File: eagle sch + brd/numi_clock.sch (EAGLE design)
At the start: 40 parts, among them IC1 MAX7219CWG, IC2 MEGA8-AI, IC4 DS1307Z, Q1 12 MHz, Q2 32kHz, X2 MINI-USB-UX60-MB-5S8

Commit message: Fixes #1
Fixes #1
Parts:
- removed C5, C6, C7, C8: 100nF, resistor:C-EUC0805
- removed C9: 27pF, resistor:C-EUC0805
- removed HC-SR505: (no value), con-lstb:MA03-1
- removed IC3: (no value), lm75:LM75_ICN
- removed IC4: DS1307Z, ds1307_pcf8583:DS1307Z
- removed Q2: 32kHz, crystal:CRYSTALHC49U-V
- removed R12: 26k, resistor:R-EU_M0805
- removed R15, R16: 10K, resistor:R-EU_M0805
- removed SV3, SV4, SV5, SV6: (no value), con-lstb:MA09-1
- removed X2: MINI-USB-UX60-MB-5S8, con-hirose:MINI-USB-UX60-MB-5S8
- added D2: 3.6V, SparkFun-DiscreteSemi:DIODE-ZENER3.3V
- added D3: red, SparkFun-LED:LED1206
- added JP1: micro-usb, SparkFun-Connectors:USB_MICROB_PLUGCONN-11752
- added SV2: HC-SR505, con-lstb:MA03-1
- added U$1: MAX7219CWG, max7219:MAX7219CWG
- added U$2: DS1307SO8, SparkFun-FreqCtrl:DS1307SO8
- added U$3, U$4, U$5, U$6: IV-9, domestichacks:IV-9
- added Y1: 32.768kHz, SparkFun-FreqCtrl:CRYSTALTC26H
- C1: value 27pF -> 100nF; device resistor:C-EUC0805 -> rcl:C-EUC0805
- C2, C4: device resistor:C-EUC0805 -> rcl:C-EUC0805
- C3: value 100nF -> 27pF; device resistor:C-EUC0805 -> rcl:C-EUC0805
- D1: value RED -> 3.6V; device display-hp:HLMP6 -> SparkFun-DiscreteSemi:DIODE-ZENER3.3V
- IC1: value MAX7219CWG -> MEGA8-AI; device max7219:MAX7219CWG -> atmel:MEGA8-AI
- IC2: value MEGA8-AI -> LM75; device atmel:MEGA8-AI -> lm75:LM75_ICN
- Q1: value 12 MHz -> 12MHz; device crystal:CRYSTALHC49U-V -> crystal:CRYSTALHC49S
- R1, R2: device resistor:R-EU_M0805 -> rcl:R-EU_R0805
- R10, R8, R9: value 10K -> 10k; device resistor:R-EU_M0805 -> rcl:R-EU_R0805
- R11: value 10K -> 23k; device resistor:R-EU_M0805 -> rcl:R-EU_R0805
- R3: value 68 -> 1.8k; device resistor:R-EU_M0805 -> rcl:R-EU_R0805
- R4: value 1.8K -> 68; device resistor:R-EU_M0805 -> rcl:R-EU_R0805
- R5, R6: value 3v6 -> 10k; device e-halbleiter:Z-DIODE -> rcl:R-EU_R0805
- R7: value 330 -> 10k; device resistor:R-EU_M0805 -> rcl:R-EU_R0805
- S1, S2: value SWITCH-MOMENTARY-2SMD -> SWITCH-MOMENTARY-2TACTILE-SWITCH-SMD-RIGHT-ANGLE; device SparkFun-Electromechanical:SWITCH-MOMENTARY-2SMD -> SparkFun-Electromechanical:SWITCH-MOMENTARY-2TACTILE-SWITCH-SMD-RIGHT-ANGLE
- SL1: value (none) -> VBATT
- SV1: value (none) -> SPI
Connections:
- removed net CLK: IC1.CLK
- removed net N$12: R1.1
- removed net N$14: C9.1, IC3.VCC
- removed net N$15: IC2.VCC@1
- removed net N$16: R11.2
- removed net N$17: IC1.ISET, R12.2
- removed net N$18: IC2.PB7(XTAL2/TOSC2)
- removed net N$19: IC2.PB6(XTAL1/TOSC1)
- removed net N$20: IC2.PD3(INT1)
- removed net N$21: R9.2
- removed net N$22: R8.1
- removed net N$23: R6.A
- removed net N$24: R5.C
- removed net N$26: R6.C
- removed net N$28: SL1.2
- removed net N$29: C2.1
- removed net N$30: D1.K, R7.1
- removed net N$31: SV1.2
- removed net N$32: R1.2
- removed net N$35: IC4.X2, Q2.1
- removed net N$36: IC4.X1, Q2.2
- removed net N$39: IC3.GND
- removed net N$42: IC1.GND@1, IC1.GND@2
- removed net N$45: SV3.6
- removed net N$48: IC3.A2
- removed net N$6: R2.1, X2.3
- new net N$10: IC1.PD3(INT1), R2.2
- new net N$8: D1.C, JP1.D-, R2.1, R3.2
- net +3V3: now also R5.1, R6.1, R7.1, R9.1, S1.1, SL1.2, U$2.VBATT; no longer IC4.VBAT, R11.1, S2.1
- net +5V: now also D3.A, IC1.AREF, IC1.AVCC, IC1.VCC@1, IC1.VCC@2, IC2.VCC, JP1.VCC, R1.2, R10.1, R11.1, R3.1, R8.1, SV1.2, SV2.1, U$1.VCC, U$2.VCC; no longer C3.2, C5.2, C6.2, C8.2, D1.A, IC1.VCC, IC2.AREF, IC2.AVCC, IC2.VCC@2, IC4.VCC, R12.1, R15.1, R16.1, R4.1, X2.1
- net A: now also U$1.SEGA, U$3.5, U$4.5, U$5.5, U$6.5; no longer IC1.SEGA, SV3.8, SV4.8, SV5.8, SV6.8
- net B: now also U$1.SEGB, U$3.3, U$4.3, U$5.3, U$6.3; no longer IC1.SEGB, SV3.7, SV4.7, SV5.7, SV6.7
- net C: now also U$1.SEGC, U$3.4, U$4.4, U$5.4, U$6.4; no longer IC1.SEGC, SV4.6, SV5.6, SV6.6
- net CS: now also IC1.PC1(ADC1), U$1.LOAD; no longer IC1.LOAD, IC2.PC1(ADC1)
- net D: now also U$1.SEGD, U$3.8, U$4.8, U$5.8, U$6.8; no longer IC1.SEGD, SV3.5, SV4.5, SV5.5, SV6.5
- net DIG0: now also R9.2, U$1.DIG0, U$6.1; no longer IC1.DIG0, SV3.9
- net DIG1: now also R7.2, U$1.DIG1, U$5.1; no longer IC1.DIG1
- net DIG2: now also R6.2, U$1.DIG2, U$4.1; no longer IC1.DIG2, SV5.9
- net DIG3: now also R5.2, U$1.DIG3, U$3.1; no longer IC1.DIG3, R8.2, SV6.9
- net DP: now also U$1.SEGDP, U$3.2, U$4.2, U$5.2, U$6.2; no longer IC1.SEGDP, SV3.1, SV4.1, SV5.1, SV6.1
- net E: now also U$1.SEGE, U$3.9, U$4.9, U$5.9, U$6.9; no longer IC1.SEGE, SV3.4, SV4.4, SV5.4, SV6.4
- net F: now also U$1.SEGF, U$3.6, U$4.6, U$5.6, U$6.6; no longer IC1.SEGF, SV3.3, SV4.3, SV5.3, SV6.3
- net G: now also U$1.SEGG, U$3.7, U$4.7, U$5.7, U$6.7; no longer IC1.SEGG, SV3.2, SV4.2, SV5.2, SV6.2
- net GND: now also C2.1, D1.A, D2.A, D3.C, IC1.GND, IC1.GND@1, IC1.GND@2, IC2.A0, IC2.A1, IC2.A2, JP1.GND, JP1.ID, SV2.3, U$1.GND@1, U$1.GND@2, U$2.GND; no longer C5.1, C6.1, C7.1, C8.1, C9.2, HC-SR505.3, IC2.GND@1, IC2.GND@2, IC3.A0, IC3.A1, IC4.GND, R5.A, R7.2
- net HC: now also IC1.PC0(ADC0), SV2.2; no longer HC-SR505.2, IC2.PC0(ADC0)
- net MISO: now also IC1.PB4(MISO)
- net MOSI: now also IC1.PB3(MOSI/OC2), U$1.DIN; no longer IC1.DIN
- net N$1: now also C2.2, IC1.PB6(XTAL1/TOSC1); no longer C1.2
- net N$2: now also C3.2, IC1.PB7(XTAL2/TOSC2); no longer C2.2
- net N$3: now also R11.2, U$1.ISET; no longer HC-SR505.1
- net N$4: now also U$2.X1, Y1.2; no longer R3.2
- net N$5: now also U$2.X2, Y1.1; no longer S1.1
- net N$7: now also D2.C, JP1.D+, R4.1; no longer R3.1, R4.2, X2.2
- net N$9: now also IC1.PD2(INT0), R4.2; no longer IC2.PD2(INT0), R2.2
- net RESET: now also C1.2, IC1.PC6(/RESET), R1.1, S2.1; no longer C7.2, IC2.PC6(/RESET)
- net SCK: now also IC1.PB5(SCK), U$1.CLK
- net SCL: now also IC2.SCL, R10.2, U$2.SCL; no longer IC2.PC5(ADC5/SCL), IC3.SCL, IC4.SCL, R16.2
- net SDA: now also IC2.SDA, R8.2, U$2.SDA; no longer IC2.PC4(ADC4/SDA), IC3.SDA, IC4.SDA, R15.2
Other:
- moved on the sheet: C1, C2, C3, C4, Q1, R1, R10, R11, R2, R3, R4, R7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

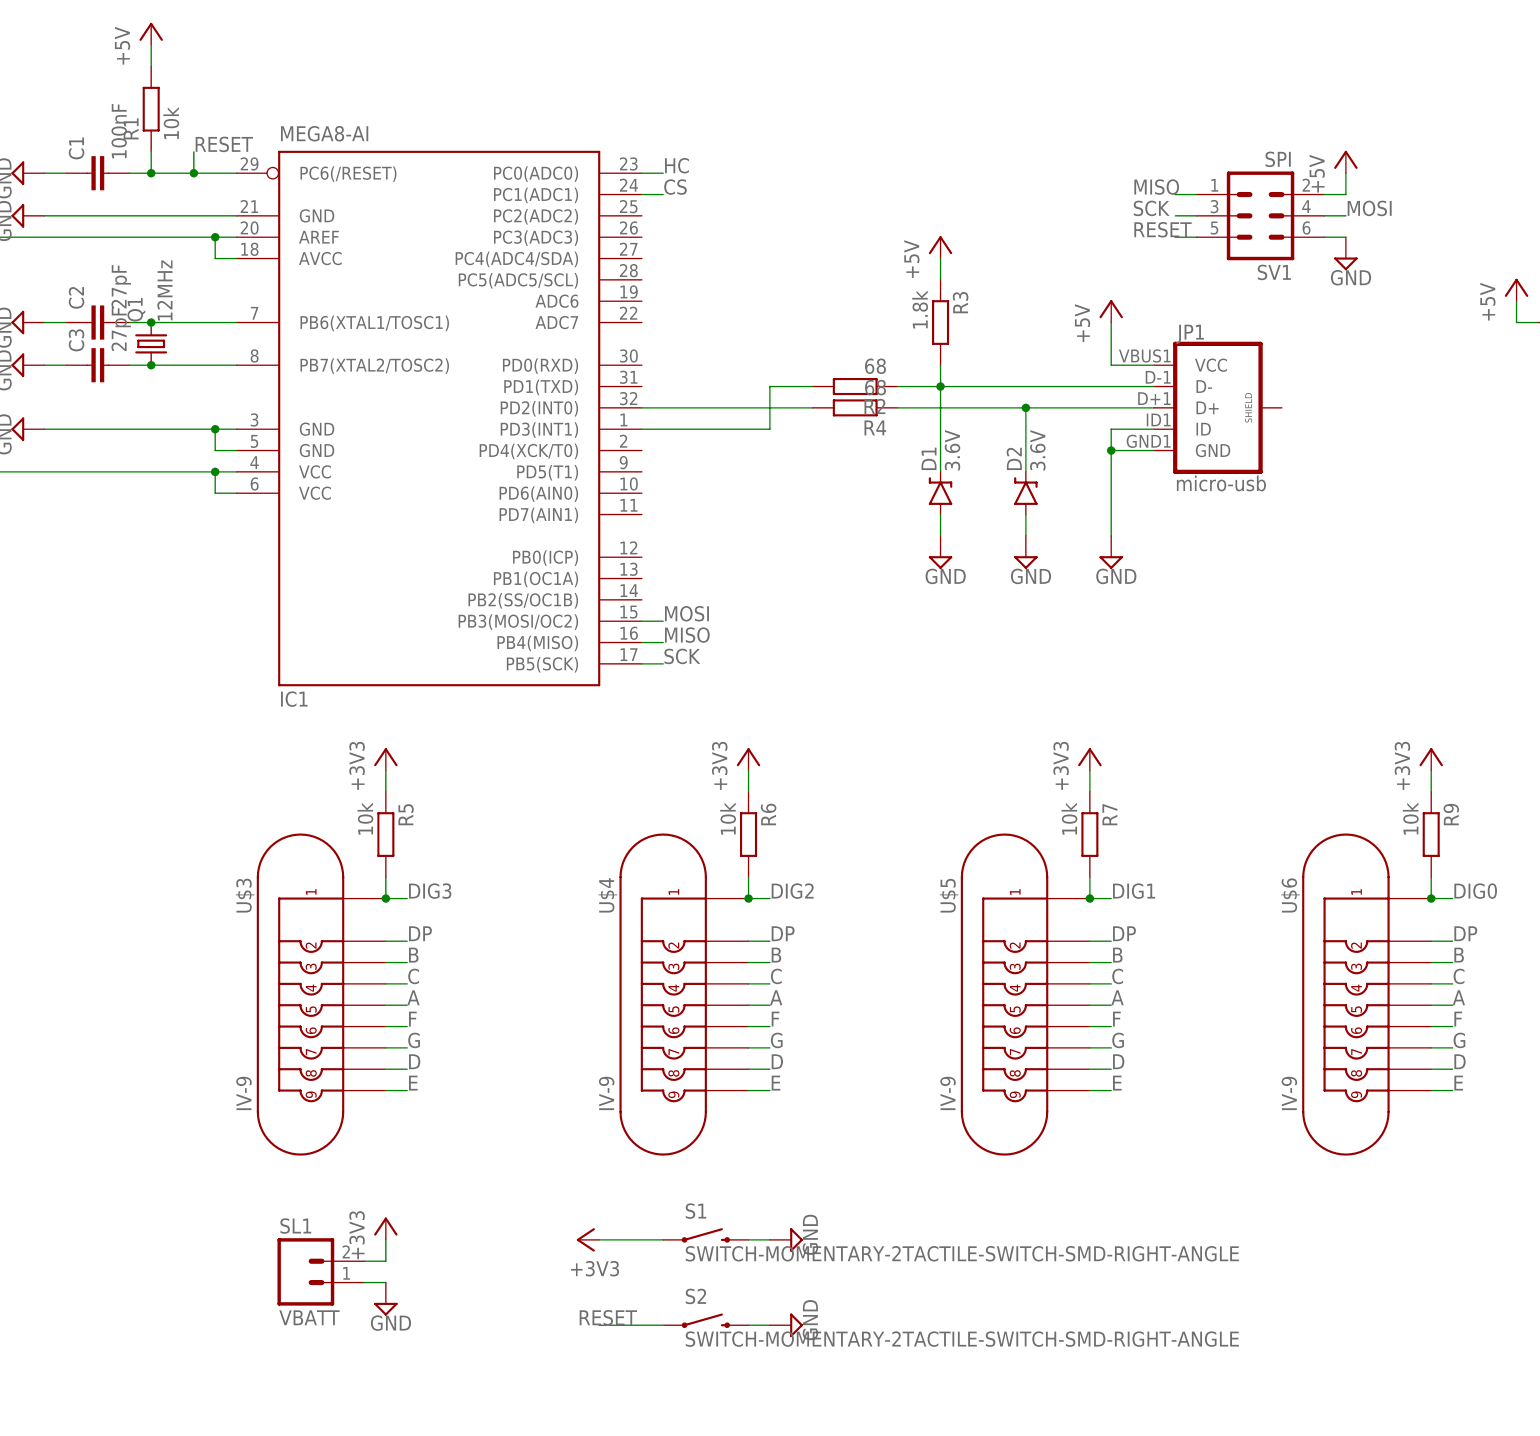
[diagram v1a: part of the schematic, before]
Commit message: added buttons for hour, minute, function
added buttons for hour, minute, function
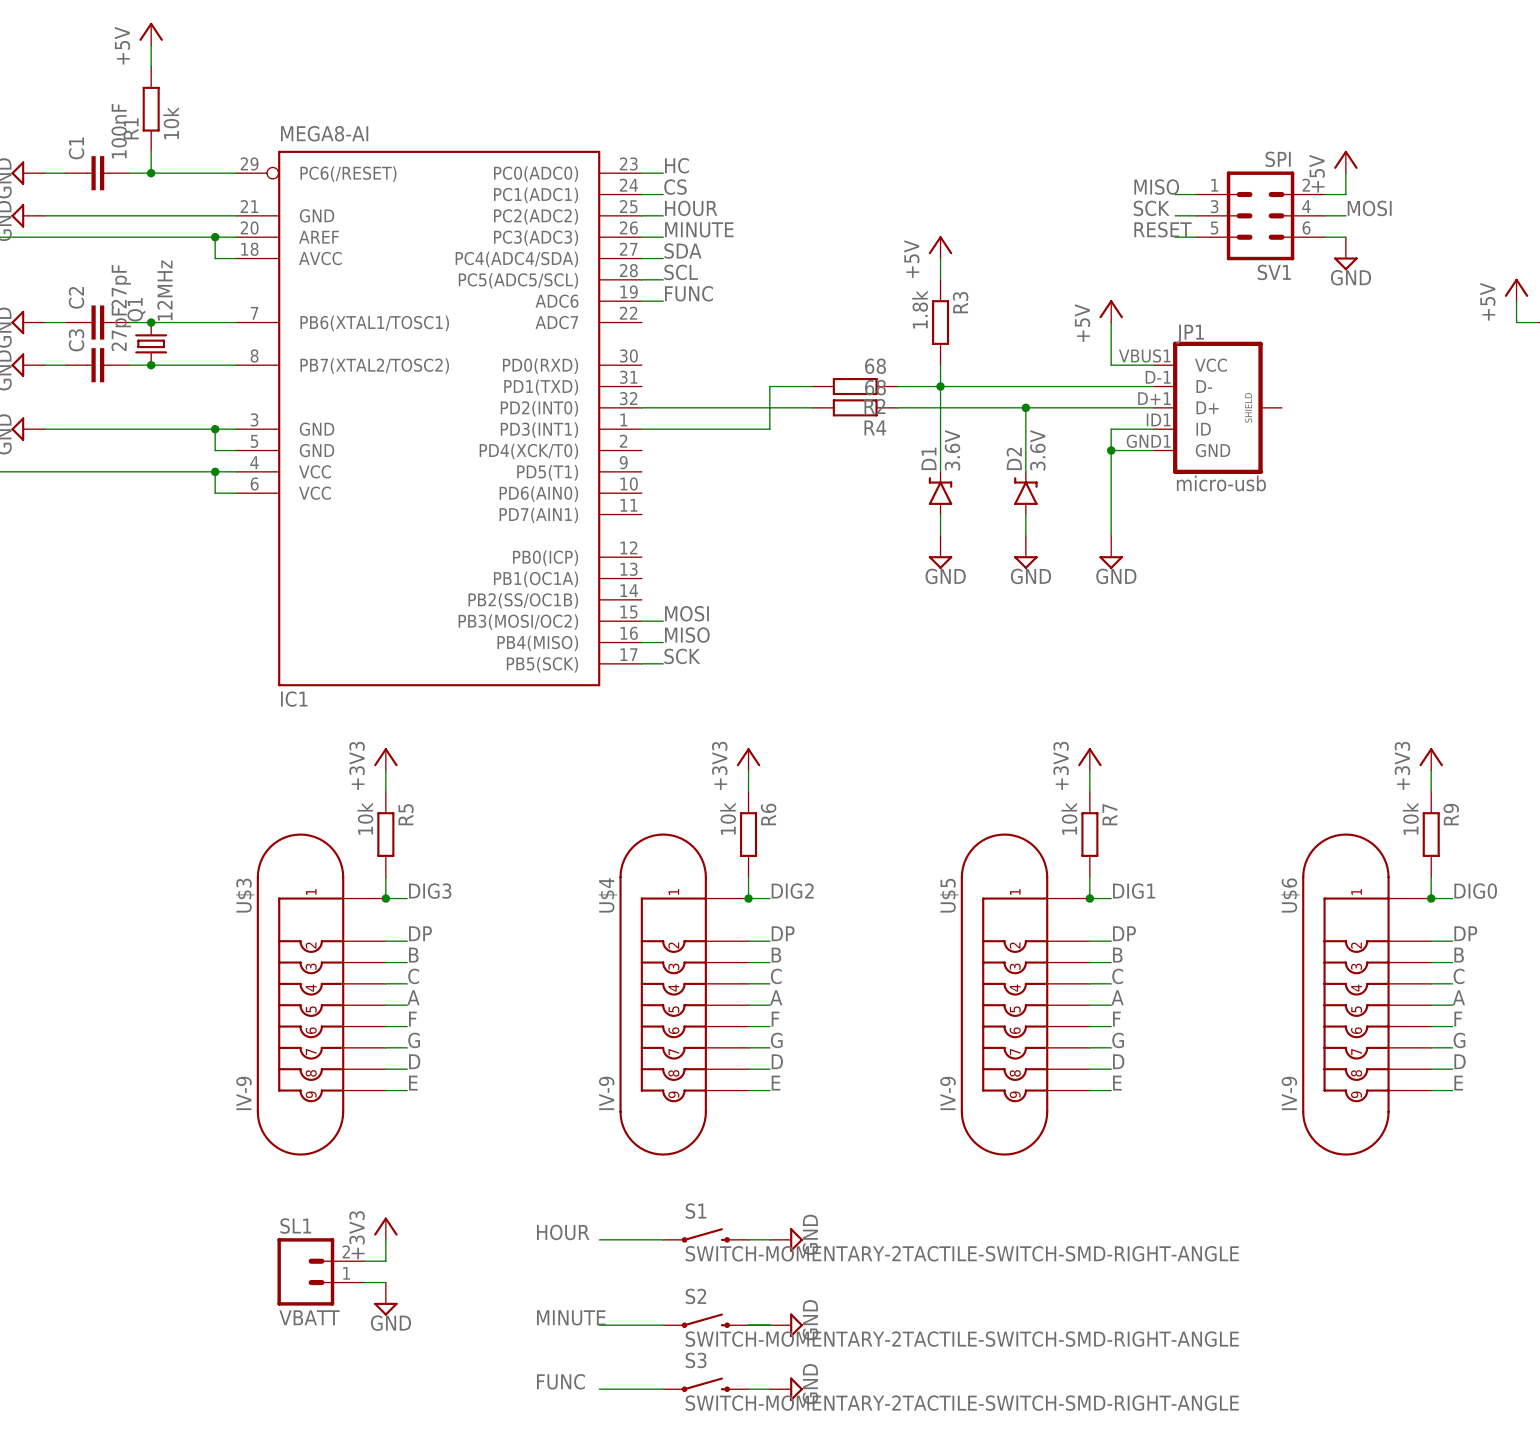
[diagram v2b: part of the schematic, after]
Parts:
- added S3: SWITCH-MOMENTARY-2TACTILE-SWITCH-SMD-RIGHT-ANGLE, SparkFun-Electromechanical:SWITCH-MOMENTARY-2TACTILE-SWITCH-SMD-RIGHT-ANGLE
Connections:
- new net FUNC: IC1.ADC6, S3.1
- new net HOUR: IC1.PC2(ADC2), S1.1
- new net MINUTE: IC1.PC3(ADC3), S2.1
- net +3V3: no longer S1.1
- net GND: now also S3.2
- net RESET: no longer S2.1
- net SCL: now also IC1.PC5(ADC5/SCL)
- net SDA: now also IC1.PC4(ADC4/SDA)
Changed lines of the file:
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@@
 <part name="S1" library="SparkFun-Electromechanical" deviceset="SWITCH-MOMENTARY-2" device="TACTILE-SWITCH-SMD-RIGHT-ANGLE"/>
 <part name="S2" library="SparkFun-Electromechanical" deviceset="SWITCH-MOMENTARY-2" device="TACTILE-SWITCH-SMD-RIGHT-ANGLE"/>
-<part name="+3V7" library="supply1" deviceset="+3V3" device=""/>
 <part name="SUPPLY17" library="supply2" deviceset="GND" device=""/>
 <part name="SUPPLY18" library="supply2" deviceset="GND" device=""/>
 <part name="R11" library="rcl" deviceset="R-EU_" device="R0805" value="23k"/>
 <part name="P+13" library="supply1" deviceset="+5V" device=""/>
+<part name="S3" library="SparkFun-Electromechanical" deviceset="SWITCH-MOMENTARY-2" device="TACTILE-SWITCH-SMD-RIGHT-ANGLE"/>
+<part name="SUPPLY19" library="supply2" deviceset="GND" device=""/>
 </parts>
 <sheets>
@@
 <instance part="S1" gate="G$1" x="-71.12" y="17.78"/>
 <instance part="S2" gate="G$1" x="-71.12" y="7.62"/>
-<instance part="+3V7" gate="G$1" x="-86.36" y="17.78" rot="R90"/>
 <instance part="SUPPLY17" gate="GND" x="-60.96" y="17.78" rot="R90"/>
 <instance part="SUPPLY18" gate="GND" x="-60.96" y="7.62" rot="R90"/>
 <instance part="R11" gate="G$1" x="33.02" y="127"/>
 <instance part="P+13" gate="1" x="25.4" y="132.08"/>
+<instance part="S3" gate="G$1" x="-71.12" y="0"/>
+<instance part="SUPPLY19" gate="GND" x="-60.96" y="0" rot="R90"/>
 </instances>
 <busses>
@@
 <pinref part="SUPPLY18" gate="GND" pin="GND"/>
 <wire x1="-66.04" y1="7.62" x2="-63.5" y2="7.62" width="0.1524" layer="91"/>
+<wire x1="-66.04" y1="7.62" x2="-63.5" y2="7.62" width="0.1524" layer="91"/>
+</segment>
+<segment>
+<pinref part="SUPPLY19" gate="GND" pin="GND"/>
+<pinref part="S3" gate="G$1" pin="2"/>
+<wire x1="-63.5" y1="0" x2="-66.04" y2="0" width="0.1524" layer="91"/>
 </segment>
 </net>
@@
 </segment>
 <segment>
-<pinref part="S2" gate="G$1" pin="1"/>
-<wire x1="-76.2" y1="7.62" x2="-83.82" y2="7.62" width="0.1524" layer="91"/>
-<label x="-86.36" y="7.62" size="1.778" layer="95"/>
-</segment>
-<segment>
 <pinref part="C1" gate="G$1" pin="2"/>
 <pinref part="IC1" gate="G$1" pin="PC6(/RESET)"/>
 <wire x1="-139.7" y1="144.78" x2="-137.16" y2="144.78" width="0.1524" layer="91"/>
 <pinref part="R1" gate="G$1" pin="1"/>
-<wire x1="-137.16" y1="144.78" x2="-132.08" y2="144.78" width="0.1524" layer="91"/>
-<wire x1="-132.08" y1="144.78" x2="-127" y2="144.78" width="0.1524" layer="91"/>
+<wire x1="-137.16" y1="144.78" x2="-127" y2="144.78" width="0.1524" layer="91"/>
 <wire x1="-137.16" y1="147.32" x2="-137.16" y2="144.78" width="0.1524" layer="91"/>
-<wire x1="-132.08" y1="144.78" x2="-132.08" y2="147.32" width="0.1524" layer="91"/>
-<label x="-132.08" y="147.32" size="1.778" layer="95"/>
-<junction x="-132.08" y="144.78"/>
 <junction x="-137.16" y="144.78"/>
 </segment>
@@
 <label x="78.74" y="50.8" size="1.778" layer="95" rot="R90"/>
 </segment>
+<segment>
+<pinref part="IC1" gate="G$1" pin="PC4(ADC4/SDA)"/>
+<wire x1="-78.74" y1="134.62" x2="-76.2" y2="134.62" width="0.1524" layer="91"/>
+<label x="-76.2" y="134.62" size="1.778" layer="95"/>
+</segment>
 </net>
 <net name="SCL" class="0">
@@
 <wire x1="86.36" y1="58.42" x2="86.36" y2="53.34" width="0.1524" layer="91"/>
 <label x="88.9" y="50.8" size="1.778" layer="95" rot="R90"/>
+</segment>
+<segment>
+<pinref part="IC1" gate="G$1" pin="PC5(ADC5/SCL)"/>
+<wire x1="-78.74" y1="132.08" x2="-76.2" y2="132.08" width="0.1524" layer="91"/>
+<label x="-76.2" y="132.08" size="1.778" layer="95"/>
 </segment>
 </net>
@@
 <wire x1="-111.76" y1="15.24" x2="-109.22" y2="15.24" width="0.1524" layer="91"/>
 <wire x1="-109.22" y1="15.24" x2="-109.22" y2="17.78" width="0.1524" layer="91"/>
-</segment>
-<segment>
-<pinref part="+3V7" gate="G$1" pin="+3V3"/>
-<pinref part="S1" gate="G$1" pin="1"/>
-<wire x1="-83.82" y1="17.78" x2="-76.2" y2="17.78" width="0.1524" layer="91"/>
 </segment>
 <segment>
@@
 </segment>
 </net>
+<net name="HOUR" class="0">
+<segment>
+<pinref part="S1" gate="G$1" pin="1"/>
+<wire x1="-83.82" y1="17.78" x2="-76.2" y2="17.78" width="0.1524" layer="91"/>
+<label x="-91.44" y="17.78" size="1.778" layer="95"/>
+</segment>
+<segment>
+<pinref part="IC1" gate="G$1" pin="PC2(ADC2)"/>
+<wire x1="-78.74" y1="139.7" x2="-76.2" y2="139.7" width="0.1524" layer="91"/>
+<label x="-76.2" y="139.7" size="1.778" layer="95"/>
+</segment>
+</net>
+<net name="FUNC" class="0">
+<segment>
+<pinref part="S3" gate="G$1" pin="1"/>
+<wire x1="-76.2" y1="0" x2="-83.82" y2="0" width="0.1524" layer="91"/>
+<label x="-91.44" y="0" size="1.778" layer="95"/>
+</segment>
+<segment>
+<pinref part="IC1" gate="G$1" pin="ADC6"/>
+<wire x1="-78.74" y1="129.54" x2="-76.2" y2="129.54" width="0.1524" layer="91"/>
+<label x="-76.2" y="129.54" size="1.778" layer="95"/>
+</segment>
+</net>
+<net name="MINUTE" class="0">
+<segment>
+<pinref part="S2" gate="G$1" pin="1"/>
+<wire x1="-76.2" y1="7.62" x2="-83.82" y2="7.62" width="0.1524" layer="91"/>
+<label x="-91.44" y="7.62" size="1.778" layer="95"/>
+</segment>
+<segment>
+<pinref part="IC1" gate="G$1" pin="PC3(ADC3)"/>
+<wire x1="-78.74" y1="137.16" x2="-76.2" y2="137.16" width="0.1524" layer="91"/>
+<label x="-76.2" y="137.16" size="1.778" layer="95"/>
+</segment>
+</net>

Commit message: minor changes
minor changes
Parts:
- removed SL1: VBATT, con-amp-quick:MA02
- added BAT2: cr2032, SparkFun:BATTERY20PTH
- added C5, C6, C7, C8: 100nF, rcl:C-EUC0805
- added D4: red, SparkFun-LED:LED1206
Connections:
- removed net +3V3: R5.1, R6.1, R7.1, R9.1, SL1.2, U$2.VBATT
- new net LED: D4.A, IC1.ADC7
- new net N$6: BAT2.+, U$2.VBATT
- net +5V: now also C5.2, C6.2, C7.2, C8.2, R5.1, R6.1, R7.1, R9.1
- net GND: now also BAT2.-, C5.1, C6.1, C7.1, C8.1, D4.C; no longer SL1.1

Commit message: layout adjustments
layout adjustments
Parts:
- removed R5, R6, R7: 10k, rcl:R-EU_R0805
- removed U$3, U$4, U$5, U$6: IV-9, domestichacks:IV-9
- added C10, C9: 27pF, rcl:C-EUC0805
- added SV7: dig0, con-lstb:MA09-1
- added SV8: conn digits, con-lstb:MA04-1
- C2, C3: value 27pF -> 22pF
- Q1: device crystal:CRYSTALHC49S -> crystal:CRYSTALCTS406
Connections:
- net +5V: no longer R5.1, R6.1, R7.1
- net A: now also SV7.5; no longer U$3.5, U$4.5, U$5.5, U$6.5
- net B: now also SV7.3; no longer U$3.3, U$4.3, U$5.3, U$6.3
- net C: now also SV7.4; no longer U$3.4, U$4.4, U$5.4, U$6.4
- net D: now also SV7.8; no longer U$3.8, U$4.8, U$5.8, U$6.8
- net DIG0: now also SV7.1, SV8.1; no longer U$6.1
- net DIG1: now also SV8.2; no longer R7.2, U$5.1
- net DIG2: now also SV8.3; no longer R6.2, U$4.1
- net DIG3: now also SV8.4; no longer R5.2, U$3.1
- net DP: now also SV7.2; no longer U$3.2, U$4.2, U$5.2, U$6.2
- net E: now also SV7.9; no longer U$3.9, U$4.9, U$5.9, U$6.9
- net F: now also SV7.6; no longer U$3.6, U$4.6, U$5.6, U$6.6
- net G: now also SV7.7; no longer U$3.7, U$4.7, U$5.7, U$6.7
- net GND: now also C10.1, C9.1; no longer JP1.ID
- net N$4: now also C9.2, Y1.1; no longer Y1.2
- net N$5: now also C10.2, Y1.2; no longer Y1.1
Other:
- moved on the sheet: R9, Y1
